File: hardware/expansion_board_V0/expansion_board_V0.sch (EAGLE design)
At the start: 550 parts, among them CON1 M2, CON10 QEI3, CON11 QEI2, CON12 CON14, CON13 UART1, CON14 UART0, CON15 BALISE, CON2 TELEM, CON28 NC, CON3 M5, CON4 M3, CON5 M4, CON6 M0, CON7 M1, CON8 QEI1, CON9 QEI0, IC1 REF5025I, IC2 REF5030I, J1 0, J10 0, J100 JUMP_402, J101 JUMP_402, J102 JUMP_402, J103 JUMP_402, J104 JUMP_402, J105 JUMP_402, J106 JUMP_402, J107 JUMP_402, J108 JUMP_402, J109 JUMP_402, J11 0, J110 JUMP_402, J111 JUMP_402, J112 JUMP_402, J113 JUMP_402, J114 JUMP_402, J115 JUMP_402, J116 JUMP_402, J117 JUMP_402, J118 JUMP_402, J119 nc, J12 0, J120 0, J121 nc, J122 0, J123 nc, J124 0, J125 nc, J126 0, J127 nc, J128 0, J129 nc, J13 0, J130 0, J131 nc, J132 0, J14 0, J15 0, J16 0, J17 0, J19 0, J2 0, J20 nc, J21 0, J22 0, J23 0, J24 nc, J25 nc, J26 JUMP_402, J27 JUMP_402, J28 nc, J29 0, J3 0, J30 0, J31 nc, J32 0, J33 0, J34 0, J35 JUMP_402, J36 JUMP_402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

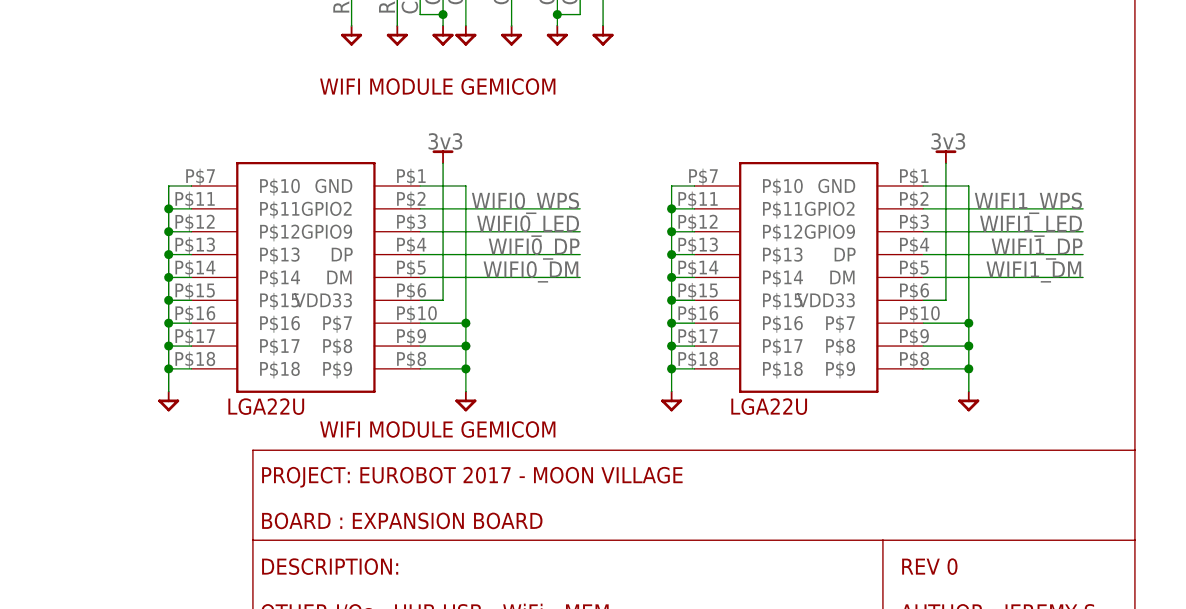
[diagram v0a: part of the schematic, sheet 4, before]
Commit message: Add Gemicom lib + update module in sch/brd
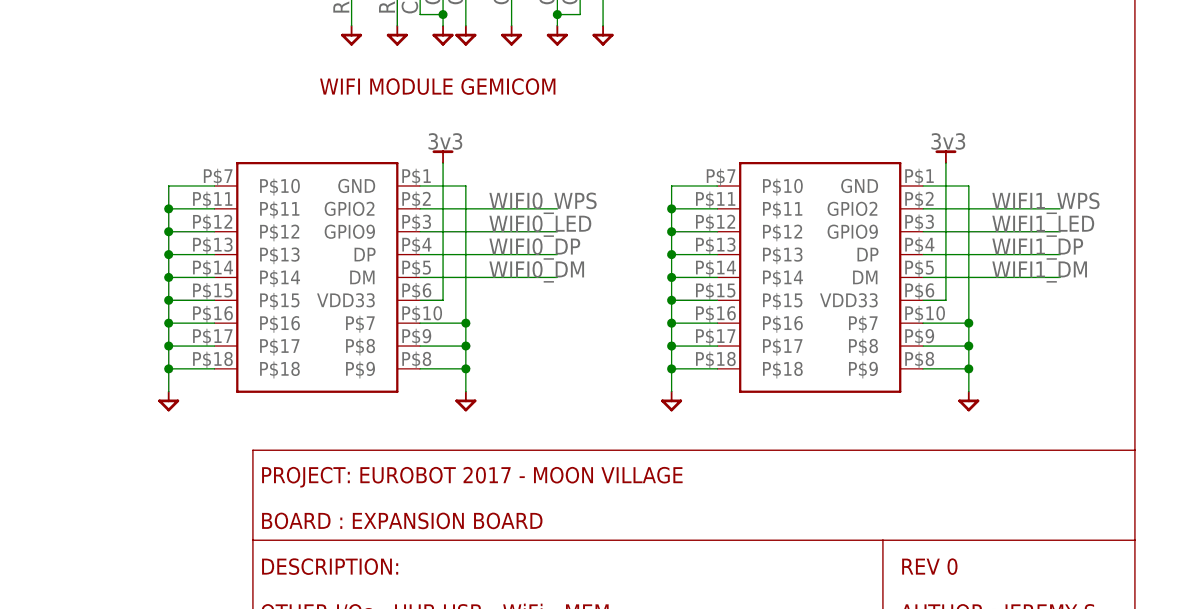
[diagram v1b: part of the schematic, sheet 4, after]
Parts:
- removed U$12, U$35: LGA22U, Gemicom:LGA22U
- added U$5, U$6: LGA22U, Gemicom:LGA22U
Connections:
- net 3V3: now also U$5.VDD33, U$6.VDD33; no longer U$12.VDD33, U$35.VDD33
- net GND: now also U$5.GND, U$5.P$10, U$5.P$11, U$5.P$12, U$5.P$13, U$5.P$14, U$5.P$15, U$5.P$16, U$5.P$17, U$5.P$18, U$5.P$7, U$5.P$8, U$5.P$9, U$6.GND, U$6.P$10, U$6.P$11, U$6.P$12, U$6.P$13, U$6.P$14, U$6.P$15, U$6.P$16, U$6.P$17, U$6.P$18, U$6.P$7, U$6.P$8, U$6.P$9; no longer U$12.GND, U$12.P$10, U$12.P$11, U$12.P$12, U$12.P$13, U$12.P$14, U$12.P$15, U$12.P$16, U$12.P$17, U$12.P$18, U$12.P$7, U$12.P$8, U$12.P$9, U$35.GND, U$35.P$10, U$35.P$11, U$35.P$12, U$35.P$13, U$35.P$14, U$35.P$15, U$35.P$16, U$35.P$17, U$35.P$18, U$35.P$7, U$35.P$8, U$35.P$9
- net WIFI0_DM: now also U$5.DM; no longer U$12.DM
- net WIFI0_DP: now also U$5.DP; no longer U$12.DP
- net WIFI0_LED: now also U$5.GPIO9; no longer U$12.GPIO9
- net WIFI0_WPS: now also U$5.GPIO2; no longer U$12.GPIO2
- net WIFI1_DM: now also U$6.DM; no longer U$35.DM
- net WIFI1_DP: now also U$6.DP; no longer U$35.DP
- net WIFI1_LED: now also U$6.GPIO9; no longer U$35.GPIO9
- net WIFI1_WPS: now also U$6.GPIO2; no longer U$35.GPIO2
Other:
- note removed: "Vérifier la footprint"

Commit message: -
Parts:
- added CON16, CON17: CON10_2_2.54, iocene:CON10_2_2.54
- added J133: NC, iocene:JUMP_603
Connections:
- net 12V: now also J133.2
- net 5V: now also CON16.9, CON17.9
- net A12V: now also J133.1
- net A5V: now also CON16.2, CON17.2
- net AD0_VREF: now also CON16.10, CON17.10
- net ESC0_CS: now also CON16.7, CON17.7
- net ESC0_DIR°: now also CON16.3, CON17.3
- net ESC0_PWM°: now also CON16.5, CON17.5
- net ESC1_CS: now also CON16.8, CON17.8
- net ESC1_DIR°: now also CON16.4, CON17.4
- net ESC1_PWM°: now also CON16.1, CON17.1
- net GND: now also CON16.6, CON17.6

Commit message: -
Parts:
- removed C159: 100n, iocene:C_402
- removed C171: 10n, iocene:C_402
- removed D2: LED_603, iocene:LED_603
- removed R107: 330, iocene:R_402
- added D8, D9: LED_603, iocene:LED_603
- added J134, J135: JUMP_402, iocene:JUMP_402
- added R1, R2: 560, iocene:R_402
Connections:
- removed net N$203: D2.A, R107.P$2
- new net AD0_VREF*: C174.P$2, C180.P$2, CON16.10, U$31.REF1, U$31.REF2, U$34.REF1, U$34.REF2
- new net ESC0_CS*: CON16.7, R93.P$2
- new net ESC0_DIR°*: CON16.3, T1.G
- new net ESC0_PWM°*: CON16.5, U14.PWM
- new net ESC1_CS*: CON16.8, R95.P$2
- new net ESC1_DIR°*: CON16.4, T2.G
- new net ESC1_PWM°*: CON16.1, U16.PWM
- new net LEDA: J134.1, R2.P$1
- new net LEDB: J135.1, R1.P$1
- new net N$61: D8.A, R1.P$2
- new net N$64: D9.A, R2.P$2
- net 12V: now also R112.P$1; no longer J31.1, R116.P$1
- net 24V: now also R116.P$1; no longer R114.P$1
- net 3V3: no longer R107.P$1
- net 5V: no longer C210.P$1, U20.VCC
- net A12V: now also J31.1
- net A5V: now also R114.P$1; no longer R112.P$1
- net AD0_VREF: no longer C171.P$2, C174.P$2, C180.P$2, CON16.10, U$31.REF1, U$31.REF2, U$34.REF1, U$34.REF2, UV1.AINN1
- net BALISE: now also U$10.A8
- net BALISE°: now also U$10.B8
- net BUZZER: now also U$10.A2; no longer U$10.A5
- net BUZZER°: now also U$10.B2; no longer U$10.B5
- net D3V3: now also C210.P$1, U20.VCC; no longer C159.P$2
- net ESC0_CS: now also C179.P$2, UV1.AINP3; no longer C173.P$2, CON16.7, R93.P$2, UV1.AINP6
- net ESC0_DIR: now also U$10.A5; no longer U$10.A2
- net ESC0_DIR°: now also U$10.B5; no longer CON16.3, T1.G, U$10.B2
- net ESC0_PWM: now also U$10.A6; no longer U$10.A1
- net ESC0_PWM°: now also U$10.B6; no longer CON16.5, U$10.B1, U14.PWM
- net ESC1_CS: now also C173.P$2, UV1.AINP2; no longer C179.P$2, CON16.8, R95.P$2, UV1.AINP7
- net ESC1_DIR: now also U$10.A4; no longer U$10.A8
- net ESC1_DIR°: now also U$10.B4; no longer CON16.4, T2.G, U$10.B8
- net ESC1_PWM: now also U$10.A3; no longer U$10.A7
- net ESC1_PWM°: now also U$10.B3; no longer CON16.1, U$10.B7, U16.PWM
- net GND: now also D8.C, D9.C, UV1.AINN1; no longer C159.P$1, C171.P$1, D2.C
- net LOW_VOLTAGE: now also UV1.AINP1; no longer UV1.AINP8
- net M0_CS: now also UV1.AINP7; no longer UV1.AINP1
- net M1_CS: now also UV1.AINP8; no longer UV1.AINP2
- net M2_CS: now also UV1.AINP6; no longer UV1.AINP3
- net M3_CS: now also UV1.AINP5; no longer UV1.AINP4
- net M4_CS: now also UV1.AINP4; no longer UV1.AINP5
- net TELEM: now also U$10.A1
- net TELEM°: now also U$10.B1
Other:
- moved on the sheet: C172, C173, C174, C178, C179, C180, C20, C22, C87, CON16, CON17, D6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

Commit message: -
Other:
- note added: "A supprimer ou à connecter ?"

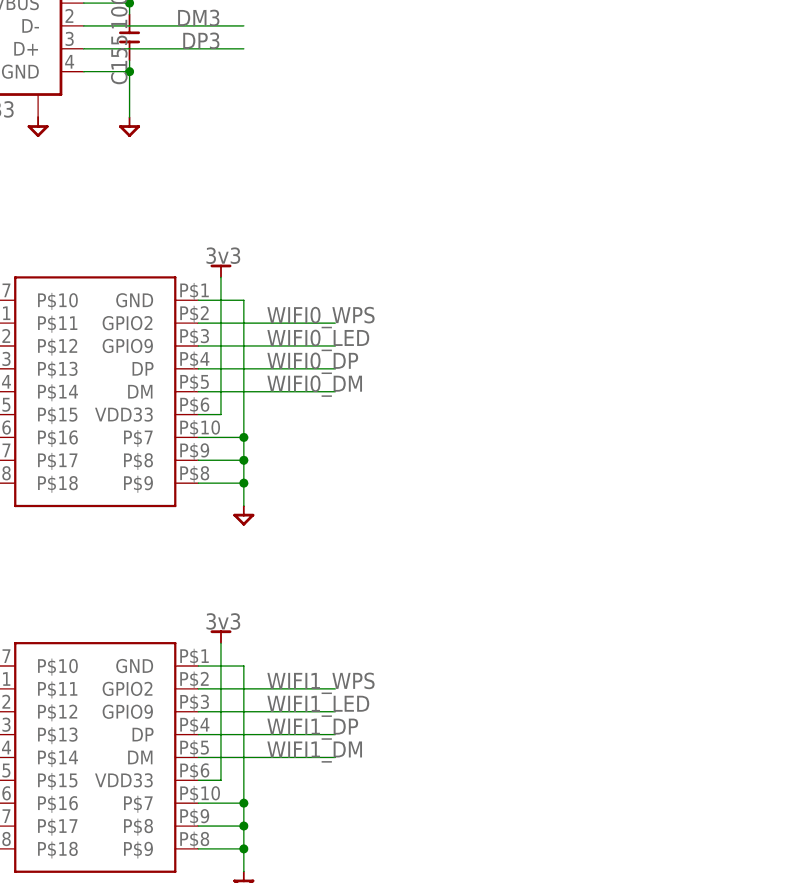
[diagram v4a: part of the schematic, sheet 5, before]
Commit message: Update WPS and LED on WiFi module
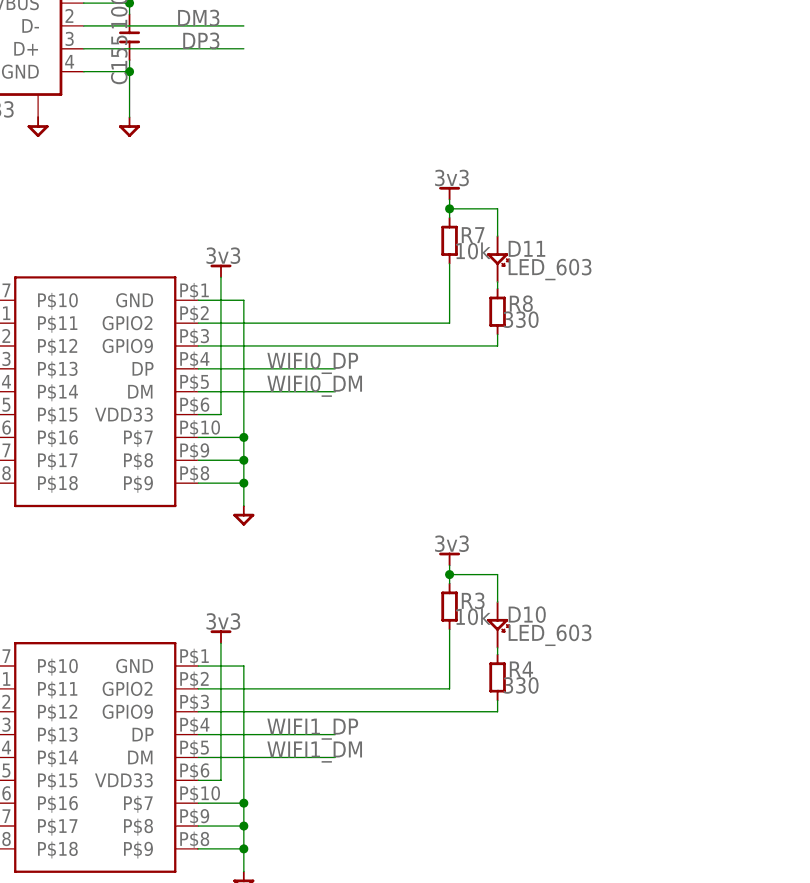
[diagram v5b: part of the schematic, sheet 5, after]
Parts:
- removed J117, J96: JUMP_402, iocene:JUMP_402
- added D10, D11: LED_603, iocene:LED_603
- added R3, R7: 10k, iocene:R_402
- added R4, R8: 330, iocene:R_402
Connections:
- removed net WIFI0_LED: U$5.GPIO9
- removed net WIFI0_WPS: J96.1, U$5.GPIO2
- new net N$66: D10.C, R4.P$2
- new net N$67: D11.C, R8.P$2
- new net WIFI1_LED1: R8.P$1, U$5.GPIO9
- new net WIFI1_WPS1: R7.P$1, U$5.GPIO2
- net 3V3: now also D10.A, D11.A, R3.P$2, R7.P$2
- net WIFI1_LED: now also R4.P$1
- net WIFI1_WPS: now also R3.P$1; no longer J117.1
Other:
- note removed: "A supprimer ou à connecter ?"
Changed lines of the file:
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@@
 <?xml version="1.0" encoding="utf-8"?>
 <!DOCTYPE eagle SYSTEM "eagle.dtd">
-<eagle version="7.2.0">
+<eagle version="7.3.0">
 <drawing>
 <settings>
@@
 <part name="J115" library="iocene" deviceset="JUMP" device="_402"/>
 <part name="J116" library="iocene" deviceset="JUMP" device="_402"/>
-<part name="J96" library="iocene" deviceset="JUMP" device="_402"/>
-<part name="J117" library="iocene" deviceset="JUMP" device="_402"/>
 <part name="J118" library="iocene" deviceset="JUMP" device="_402"/>
 <part name="5V24" library="iocene" deviceset="5V" device=""/>
@@
 <part name="J134" library="iocene" deviceset="JUMP" device="_402"/>
 <part name="J135" library="iocene" deviceset="JUMP" device="_402"/>
+<part name="3V2" library="iocene" deviceset="3V3" device=""/>
+<part name="R3" library="iocene" deviceset="R" device="_402" value="10k"/>
+<part name="R4" library="iocene" deviceset="R" device="_402" value="330"/>
+<part name="D10" library="iocene" deviceset="LED" device="_603"/>
+<part name="3V4" library="iocene" deviceset="3V3" device=""/>
+<part name="R7" library="iocene" deviceset="R" device="_402" value="10k"/>
+<part name="R8" library="iocene" deviceset="R" device="_402" value="330"/>
+<part name="D11" library="iocene" deviceset="LED" device="_603"/>
 </parts>
 <sheets>
@@
 <instance part="5V58" gate="G$1" x="43.18" y="175.26"/>
 <instance part="5V59" gate="G$1" x="43.18" y="152.4"/>
+<instance part="3V2" gate="G$1" x="78.74" y="87.376"/>
+<instance part="R3" gate="G$1" x="78.74" y="82.804" smashed="yes" rot="R180">
+<attribute name="NAME" x="82.804" y="84.328" size="1.778" layer="95" rot="R180"/>
+<attribute name="VALUE" x="79.248" y="80.772" size="1.778" layer="96"/>
+</instance>
+<instance part="R4" gate="G$1" x="84.074" y="74.93" smashed="yes" rot="R180">
+<attribute name="NAME" x="88.138" y="76.708" size="1.778" layer="95" rot="R180"/>
+<attribute name="VALUE" x="84.582" y="73.152" size="1.778" layer="96"/>
+</instance>
+<instance part="D10" gate="G$1" x="84.074" y="80.772" smashed="yes">
+<attribute name="NAME" x="85.09" y="81.026" size="1.778" layer="95"/>
+<attribute name="VALUE" x="85.09" y="78.994" size="1.778" layer="96"/>
+</instance>
+<instance part="3V4" gate="G$1" x="78.74" y="128.016"/>
+<instance part="R7" gate="G$1" x="78.74" y="123.444" smashed="yes" rot="R180">
+<attribute name="NAME" x="82.804" y="124.968" size="1.778" layer="95" rot="R180"/>
+<attribute name="VALUE" x="79.248" y="121.412" size="1.778" layer="96"/>
+</instance>
+<instance part="R8" gate="G$1" x="84.074" y="115.57" smashed="yes" rot="R180">
+<attribute name="NAME" x="88.138" y="117.348" size="1.778" layer="95" rot="R180"/>
+<attribute name="VALUE" x="84.582" y="113.792" size="1.778" layer="96"/>
+</instance>
+<instance part="D11" gate="G$1" x="84.074" y="121.412" smashed="yes">
+<attribute name="NAME" x="85.09" y="121.666" size="1.778" layer="95"/>
+<attribute name="VALUE" x="85.09" y="119.634" size="1.778" layer="96"/>
+</instance>
 </instances>
 <busses>
@@
 <wire x1="50.8" y1="63.5" x2="53.34" y2="63.5" width="0.1524" layer="91"/>
 </segment>
+<segment>
+<pinref part="3V2" gate="G$1" pin="3V3"/>
+<pinref part="R3" gate="G$1" pin="P$2"/>
+<wire x1="78.74" y1="85.344" x2="78.74" y2="86.36" width="0.1524" layer="91"/>
+<pinref part="D10" gate="G$1" pin="A"/>
+<wire x1="78.74" y1="86.36" x2="78.74" y2="87.376" width="0.1524" layer="91"/>
+<wire x1="84.074" y1="86.36" x2="84.074" y2="83.312" width="0.1524" layer="91"/>
+<wire x1="78.74" y1="86.36" x2="84.074" y2="86.36" width="0.1524" layer="91"/>
+<junction x="78.74" y="86.36"/>
+</segment>
+<segment>
+<pinref part="3V4" gate="G$1" pin="3V3"/>
+<pinref part="R7" gate="G$1" pin="P$2"/>
+<wire x1="78.74" y1="125.984" x2="78.74" y2="127" width="0.1524" layer="91"/>
+<pinref part="D11" gate="G$1" pin="A"/>
+<wire x1="78.74" y1="127" x2="78.74" y2="128.016" width="0.1524" layer="91"/>
+<wire x1="84.074" y1="127" x2="84.074" y2="123.952" width="0.1524" layer="91"/>
+<wire x1="78.74" y1="127" x2="84.074" y2="127" width="0.1524" layer="91"/>
+<junction x="78.74" y="127"/>
+</segment>
 </net>
 <net name="N$110" class="0">
@@
 </segment>
 </net>
-<net name="WIFI0_WPS" class="0">
+<net name="WIFI1_WPS" class="0">
 <segment>
-<pinref part="U$5" gate="G$1" pin="GPIO2"/>
-<wire x1="50.8" y1="114.3" x2="66.04" y2="114.3" width="0.1524" layer="91"/>
-<label x="58.42" y="114.3" size="1.778" layer="95"/>
+<pinref part="U$6" gate="G$1" pin="GPIO2"/>
+<wire x1="50.8" y1="73.66" x2="78.74" y2="73.66" width="0.1524" layer="91"/>
+<pinref part="R3" gate="G$1" pin="P$1"/>
+<wire x1="78.74" y1="73.66" x2="78.74" y2="80.264" width="0.1524" layer="91"/>
 </segment>
 </net>
-<net name="WIFI0_LED" class="0">
+<net name="WIFI1_LED" class="0">
 <segment>
-<pinref part="U$5" gate="G$1" pin="GPIO9"/>
-<wire x1="50.8" y1="111.76" x2="66.04" y2="111.76" width="0.1524" layer="91"/>
-<label x="58.42" y="111.76" size="1.778" layer="95"/>
+<pinref part="U$6" gate="G$1" pin="GPIO9"/>
+<wire x1="50.8" y1="71.12" x2="84.074" y2="71.12" width="0.1524" layer="91"/>
+<wire x1="84.074" y1="71.12" x2="84.074" y2="72.39" width="0.1524" layer="91"/>
+<pinref part="R4" gate="G$1" pin="P$1"/>
 </segment>
 </net>
-<net name="WIFI1_WPS" class="0">
+<net name="N$66" class="0">
 <segment>
-<pinref part="U$6" gate="G$1" pin="GPIO2"/>
-<wire x1="50.8" y1="73.66" x2="66.04" y2="73.66" width="0.1524" layer="91"/>
-<label x="58.42" y="73.66" size="1.778" layer="95"/>
+<pinref part="R4" gate="G$1" pin="P$2"/>
+<pinref part="D10" gate="G$1" pin="C"/>
+<wire x1="84.074" y1="77.47" x2="84.074" y2="78.232" width="0.1524" layer="91"/>
 </segment>
 </net>
-<net name="WIFI1_LED" class="0">
+<net name="WIFI1_WPS1" class="0">
 <segment>
-<pinref part="U$6" gate="G$1" pin="GPIO9"/>
-<wire x1="50.8" y1="71.12" x2="66.04" y2="71.12" width="0.1524" layer="91"/>
-<label x="58.42" y="71.12" size="1.778" layer="95"/>
+<wire x1="50.8" y1="114.3" x2="78.74" y2="114.3" width="0.1524" layer="91"/>
+<pinref part="R7" gate="G$1" pin="P$1"/>
+<wire x1="78.74" y1="114.3" x2="78.74" y2="120.904" width="0.1524" layer="91"/>
+<pinref part="U$5" gate="G$1" pin="GPIO2"/>
+</segment>
+</net>
+<net name="WIFI1_LED1" class="0">
+<segment>
+<wire x1="50.8" y1="111.76" x2="84.074" y2="111.76" width="0.1524" layer="91"/>
+<wire x1="84.074" y1="111.76" x2="84.074" y2="113.03" width="0.1524" layer="91"/>
+<pinref part="R8" gate="G$1" pin="P$1"/>
+<pinref part="U$5" gate="G$1" pin="GPIO9"/>
+</segment>
+</net>
+<net name="N$67" class="0">
+<segment>
+<pinref part="R8" gate="G$1" pin="P$2"/>
+<pinref part="D11" gate="G$1" pin="C"/>
+<wire x1="84.074" y1="118.11" x2="84.074" y2="118.872" width="0.1524" layer="91"/>
 </segment>
 </net>
@@
 <text x="12.7" y="63.5" size="1.778" layer="98">Arduino I014</text>
 <text x="93.98" y="40.64" size="1.778" layer="94">LTC connector</text>
-<text x="198.12" y="71.12" size="1.778" layer="98">A supprimer ou à connecter ?</text>
 </plain>
 <instances>
@@
 <attribute name="NAME" x="259.08" y="147.32" size="1.778" layer="95" rot="R180"/>
 </instance>
-<instance part="J96" gate="G$1" x="223.52" y="63.5" smashed="yes" rot="R90">
-<attribute name="NAME" x="226.06" y="66.04" size="1.778" layer="95" rot="R180"/>
-</instance>
-<instance part="J117" gate="G$1" x="223.52" y="55.88" smashed="yes" rot="R90">
-<attribute name="NAME" x="226.06" y="58.42" size="1.778" layer="95" rot="R180"/>
-</instance>
 <instance part="J118" gate="G$1" x="220.98" y="180.34" smashed="yes" rot="R90">
 <attribute name="NAME" x="223.52" y="182.88" size="1.778" layer="95" rot="R180"/>
@@
 </segment>
 </net>
-<net name="WIFI0_WPS" class="0">
-<segment>
-<wire x1="203.2" y1="63.5" x2="220.98" y2="63.5" width="0.1524" layer="91"/>
-<label x="220.98" y="63.5" size="1.778" layer="95" rot="MR0"/>
-<pinref part="J96" gate="G$1" pin="1"/>
-</segment>
-</net>
-<net name="WIFI0_LED" class="0">
-<segment>
-<wire x1="203.2" y1="60.96" x2="220.98" y2="60.96" width="0.1524" layer="91"/>
-<label x="220.98" y="60.96" size="1.778" layer="95" rot="MR0"/>
-</segment>
-</net>
 <net name="TELEM" class="0">
 <segment>
@@
 </segment>
 </net>
-<net name="WIFI1_WPS" class="0">
-<segment>
-<wire x1="203.2" y1="55.88" x2="220.98" y2="55.88" width="0.1524" layer="91"/>
-<label x="220.98" y="55.88" size="1.778" layer="95" rot="MR0"/>
-<pinref part="J117" gate="G$1" pin="1"/>
-</segment>
-</net>
-<net name="WIFI1_LED" class="0">
-<segment>
-<wire x1="203.2" y1="53.34" x2="220.98" y2="53.34" width="0.1524" layer="91"/>
-<label x="220.98" y="53.34" size="1.778" layer="95" rot="MR0"/>
-</segment>
-</net>
